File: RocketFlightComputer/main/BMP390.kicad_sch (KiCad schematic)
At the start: 5 parts

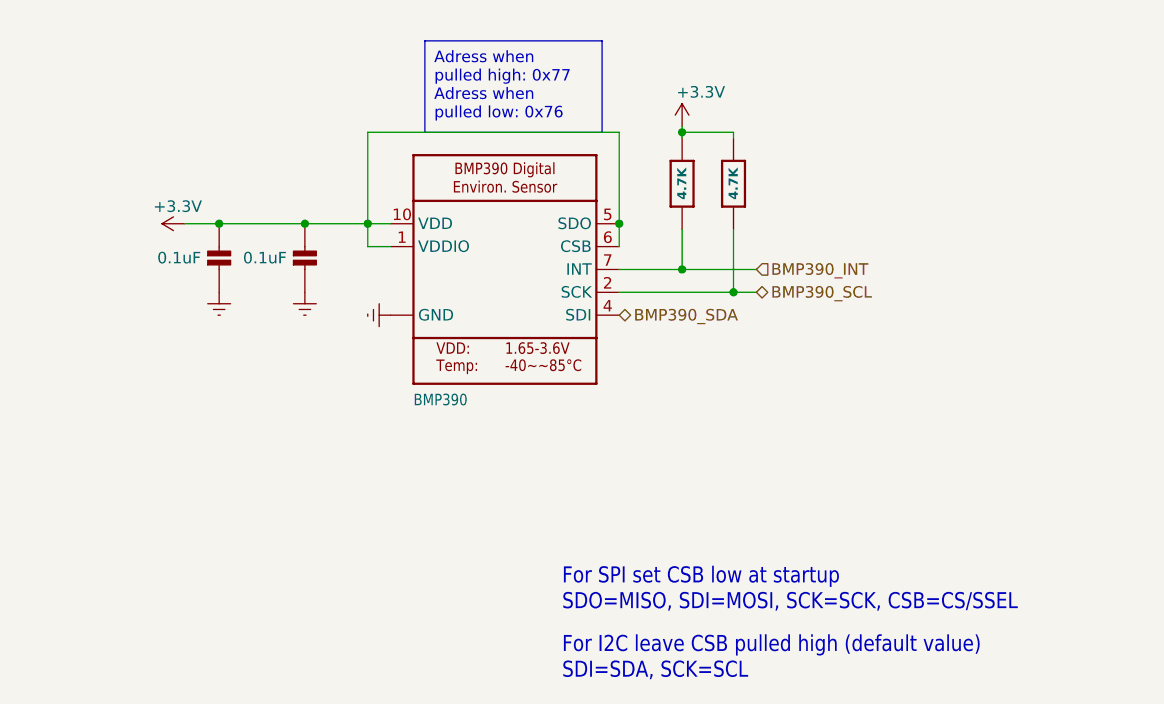
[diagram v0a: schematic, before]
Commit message: Added a few sensors schematics like multiplex for i2c comms, current/voltage sensor, micro sd slot, more to go!
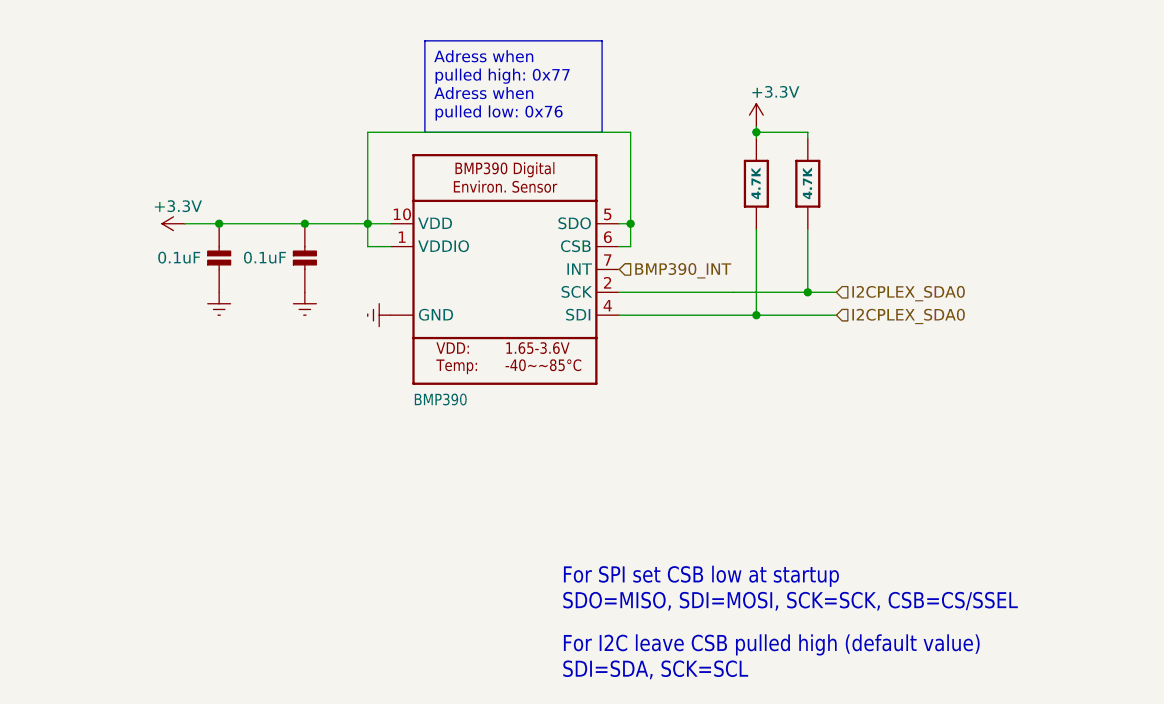
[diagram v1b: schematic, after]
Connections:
- net BMP390_SDA is gone; now on net I2CPLEX_SDA0: IC?.4 (SDI)
- net BMP390_INT: no longer R?.4 (1)
- net BMP390_SCL renamed I2CPLEX_SDA0
- net I2CPLEX_SDA0: now also R?.4 (1)
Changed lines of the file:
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@@
   (junction (at 42.545 53.34) (diameter 0) (color 0 0 0 0)
   )
-  (junction (at 86.995 53.34) (diameter 0) (color 0 0 0 0)
-  )
-  (junction (at 93.98 58.42) (diameter 0) (color 0 0 0 0)
+  (junction (at 107.95 60.96) (diameter 0) (color 0 0 0 0)
   )
   (junction (at 52.07 53.34) (diameter 0) (color 0 0 0 0)
   )
-  (junction (at 99.695 60.96) (diameter 0) (color 0 0 0 0)
-  )
   (junction (at 59.055 53.34) (diameter 0) (color 0 0 0 0)
   )
-  (junction (at 93.98 43.18) (diameter 0) (color 0 0 0 0)
+  (junction (at 88.265 53.34) (diameter 0) (color 0 0 0 0)
+  )
+  (junction (at 102.235 63.5) (diameter 0) (color 0 0 0 0)
+  )
+  (junction (at 102.235 43.18) (diameter 0) (color 0 0 0 0)
   )
   (wire (pts (xy 86.995 60.96) (xy 99.695 60.96))
     (stroke (width 0.1524) (type solid))
   )
-  (wire (pts (xy 93.98 53.975) (xy 93.98 58.42))
-    (stroke (width 0) (type default))
-  )
-  (wire (pts (xy 99.695 53.975) (xy 99.695 60.96))
-    (stroke (width 0) (type default))
-  )
-  (wire (pts (xy 93.98 58.42) (xy 102.235 58.42))
-    (stroke (width 0.1524) (type solid))
+  (wire (pts (xy 88.265 53.34) (xy 86.995 53.34))
+    (stroke (width 0) (type default))
+  )
+  (wire (pts (xy 102.235 63.5) (xy 111.125 63.5))
+    (stroke (width 0) (type default))
+  )
+  (wire (pts (xy 107.95 53.975) (xy 107.95 60.96))
+    (stroke (width 0) (type default))
   )
   (wire (pts (xy 59.055 55.88) (xy 61.595 55.88))
     (stroke (width 0.1524) (type solid))
   )
+  (wire (pts (xy 107.95 60.96) (xy 111.125 60.96))
+    (stroke (width 0) (type default))
+  )
   (wire (pts (xy 38.735 53.34) (xy 42.545 53.34))
     (stroke (width 0.1524) (type solid))
   )
-  (wire (pts (xy 86.995 43.18) (xy 59.055 43.18))
-    (stroke (width 0) (type default))
-  )
-  (wire (pts (xy 86.995 53.34) (xy 86.995 55.88))
-    (stroke (width 0) (type default))
-  )
-  (wire (pts (xy 86.995 58.42) (xy 93.98 58.42))
-    (stroke (width 0.1524) (type solid))
-  )
-  (wire (pts (xy 86.995 43.18) (xy 86.995 53.34))
-    (stroke (width 0) (type default))
-  )
-  (wire (pts (xy 93.98 43.18) (xy 93.98 43.815))
-    (stroke (width 0) (type default))
-  )
-  (wire (pts (xy 99.695 60.96) (xy 102.235 60.96))
+  (wire (pts (xy 88.265 43.18) (xy 59.055 43.18))
+    (stroke (width 0) (type default))
+  )
+  (wire (pts (xy 88.265 53.34) (xy 88.265 55.88))
+    (stroke (width 0) (type default))
+  )
+  (wire (pts (xy 88.265 43.18) (xy 88.265 53.34))
+    (stroke (width 0) (type default))
+  )
+  (wire (pts (xy 102.235 43.18) (xy 102.235 43.815))
     (stroke (width 0) (type default))
   )
@@
     (stroke (width 0.1524) (type solid))
   )
-  (wire (pts (xy 93.98 42.545) (xy 93.98 43.18))
-    (stroke (width 0) (type default))
-  )
-  (wire (pts (xy 99.695 43.18) (xy 93.98 43.18))
+  (wire (pts (xy 102.235 42.545) (xy 102.235 43.18))
+    (stroke (width 0) (type default))
+  )
+  (wire (pts (xy 107.95 43.18) (xy 102.235 43.18))
+    (stroke (width 0) (type default))
+  )
+  (wire (pts (xy 88.265 55.88) (xy 86.995 55.88))
+    (stroke (width 0) (type default))
+  )
+  (wire (pts (xy 102.235 53.975) (xy 102.235 63.5))
     (stroke (width 0) (type default))
   )
@@
     (stroke (width 0.1524) (type solid))
   )
+  (wire (pts (xy 86.995 63.5) (xy 102.235 63.5))
+    (stroke (width 0) (type default))
+  )
   (wire (pts (xy 59.055 43.18) (xy 59.055 53.34))
     (stroke (width 0) (type default))
   )
+  (wire (pts (xy 107.95 60.96) (xy 99.695 60.96))
+    (stroke (width 0) (type default))
+  )
   (wire (pts (xy 61.595 53.34) (xy 59.055 53.34))
     (stroke (width 0.1524) (type solid))
@@
     (stroke (width 0.1524) (type solid))
   )
-  (wire (pts (xy 99.695 43.815) (xy 99.695 43.18))
+  (wire (pts (xy 107.95 43.815) (xy 107.95 43.18))
     (stroke (width 0) (type default))
   )
@@
     (effects (font (size 1.778 1.5113)) (justify left bottom))
   )
-  (hierarchical_label "BMP390_INT" (shape input) (at 102.235 58.42 0) (fields_autoplaced)
+  (hierarchical_label "I2CPLEX_SDA0" (shape input) (at 111.125 60.96 0) (fields_autoplaced)
     (effects (font (size 1.27 1.27)) (justify left))
   )
-  (hierarchical_label "BMP390_SCL" (shape bidirectional) (at 102.235 60.96 0) (fields_autoplaced)
+  (hierarchical_label "BMP390_INT" (shape input) (at 86.995 58.42 0) (fields_autoplaced)
     (effects (font (size 1.27 1.27)) (justify left))
   )
-  (hierarchical_label "BMP390_SDA" (shape bidirectional) (at 86.995 63.5 0) (fields_autoplaced)
+  (hierarchical_label "I2CPLEX_SDA0" (shape input) (at 111.125 63.5 0) (fields_autoplaced)
     (effects (font (size 1.27 1.27)) (justify left))
   )
@@
     )
   )
-  (symbol (lib_id "power:+3.3V") (at 93.98 42.545 0) (unit 1)
-    (in_bom yes) (on_board yes) (dnp no)
-    (property "Reference" "#PWR063" (at 93.98 46.355 0)
-      (effects (font (size 1.27 1.27)) hide)
-    )
-    (property "Value" "+3.3V" (at 93.345 38.735 0)
+  (symbol (lib_id "power:+3.3V") (at 102.235 42.545 0) (unit 1)
+    (in_bom yes) (on_board yes) (dnp no)
+    (property "Reference" "#PWR063" (at 102.235 46.355 0)
+      (effects (font (size 1.27 1.27)) hide)
+    )
+    (property "Value" "+3.3V" (at 101.6 38.735 0)
       (effects (font (size 1.27 1.27)) (justify left))
     )
-    (property "Footprint" "" (at 93.98 42.545 0)
-      (effects (font (size 1.27 1.27)) hide)
-    )
-    (property "Datasheet" "" (at 93.98 42.545 0)
+    (property "Footprint" "" (at 102.235 42.545 0)
+      (effects (font (size 1.27 1.27)) hide)
+    )
+    (property "Datasheet" "" (at 102.235 42.545 0)
       (effects (font (size 1.27 1.27)) hide)
     )
@@
     )
   )
-  (symbol (lib_id "Adafruit_BNO08x-eagle-import:RESISTOR_4PACK") (at 93.98 48.895 90) (unit 4)
-    (in_bom yes) (on_board yes) (dnp no)
-    (property "Reference" "R?" (at 90.17 48.895 90)
-      (effects (font (size 1.27 1.27)) hide)
-    )
-    (property "Value" "4.7K" (at 93.98 48.895 0)
+  (symbol (lib_id "Adafruit_BNO08x-eagle-import:RESISTOR_4PACK") (at 102.235 48.895 90) (unit 4)
+    (in_bom yes) (on_board yes) (dnp no)
+    (property "Reference" "R?" (at 98.425 48.895 90)
+      (effects (font (size 1.27 1.27)) hide)
+    )
+    (property "Value" "4.7K" (at 102.235 48.895 0)
       (effects (font (size 1.016 1.016) bold))
     )
-    (property "Footprint" "Resistor_SMD:R_0603_1608Metric_Pad0.98x0.95mm_HandSolder" (at 93.98 48.895 0)
-      (effects (font (size 1.27 1.27)) hide)
-    )
-    (property "Datasheet" "" (at 93.98 48.895 0)
+    (property "Footprint" "Resistor_SMD:R_0603_1608Metric_Pad0.98x0.95mm_HandSolder" (at 102.235 48.895 0)
+      (effects (font (size 1.27 1.27)) hide)
+    )
+    (property "Datasheet" "" (at 102.235 48.895 0)
       (effects (font (size 1.27 1.27)) hide)
     )
@@
     )
   )
-  (symbol (lib_id "Adafruit_BNO08x-eagle-import:RESISTOR_4PACK") (at 99.695 48.895 270) (unit 3)
-    (in_bom yes) (on_board yes) (dnp no)
-    (property "Reference" "R?" (at 103.505 48.895 90)
-      (effects (font (size 1.27 1.27)) hide)
-    )
-    (property "Value" "4.7K" (at 99.695 48.895 0)
+  (symbol (lib_id "Adafruit_BNO08x-eagle-import:RESISTOR_4PACK") (at 107.95 48.895 270) (unit 3)
+    (in_bom yes) (on_board yes) (dnp no)
+    (property "Reference" "R?" (at 111.76 48.895 90)
+      (effects (font (size 1.27 1.27)) hide)
+    )
+    (property "Value" "4.7K" (at 107.95 48.895 0)
       (effects (font (size 1.016 1.016) bold))
     )
-    (property "Footprint" "Resistor_SMD:R_0603_1608Metric_Pad0.98x0.95mm_HandSolder" (at 99.695 48.895 0)
-      (effects (font (size 1.27 1.27)) hide)
-    )
-    (property "Datasheet" "" (at 99.695 48.895 0)
-      (effects (font (size 1.27 1.27)) hide)
-    )
+    (property "Footprint" "Resistor_SMD:R_0603_1608Metric_Pad0.98x0.95mm_HandSolder" (at 107.95 48.895 0)
+      (effects (font (size 1.27 1.27)) hide)
+    )
+    (property "Datasheet" "" (at 107.95 48.895 0)
+      (effects (font (size 1.27 1.27)) hide)
+    )

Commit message: Well I added a bunch of sensors, some connectors for battery, pyro channels mosfets, etc
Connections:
- net I2CPLEX_SDA0 renamed BMP390_SCL1
- net BMP390_SCL1: no longer IC?.4 (SDI), R?.4 (1)
- new net BMP390_SDA1: IC?.4 (SDI), R?.4 (1)
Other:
- note added: "Max current: 730 uA"
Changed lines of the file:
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@@
+    (effects (font (size 1.778 1.5113)) (justify left bottom))
+  )
+  (text "Max current: 730 uA\n" (at 80.645 88.9 0)
     (effects (font (size 1.778 1.5113)) (justify left bottom))
   )
@@
     (effects (font (size 1.778 1.5113)) (justify left bottom))
   )
-  (hierarchical_label "I2CPLEX_SDA0" (shape input) (at 111.125 60.96 0) (fields_autoplaced)
+  (hierarchical_label "BMP390_SCL1" (shape input) (at 111.125 60.96 0) (fields_autoplaced)
     (effects (font (size 1.27 1.27)) (justify left))
   )
@@
     (effects (font (size 1.27 1.27)) (justify left))
   )
-  (hierarchical_label "I2CPLEX_SDA0" (shape input) (at 111.125 63.5 0) (fields_autoplaced)
+  (hierarchical_label "BMP390_SDA1" (shape input) (at 111.125 63.5 0) (fields_autoplaced)
     (effects (font (size 1.27 1.27)) (justify left))
   )

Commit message: Addition of telemetry is pcb schematic
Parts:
- gave numbers to parts that had none: 4
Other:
- note added: "Max current: 0.73mA"
- note removed: "Max current: 730 uA"

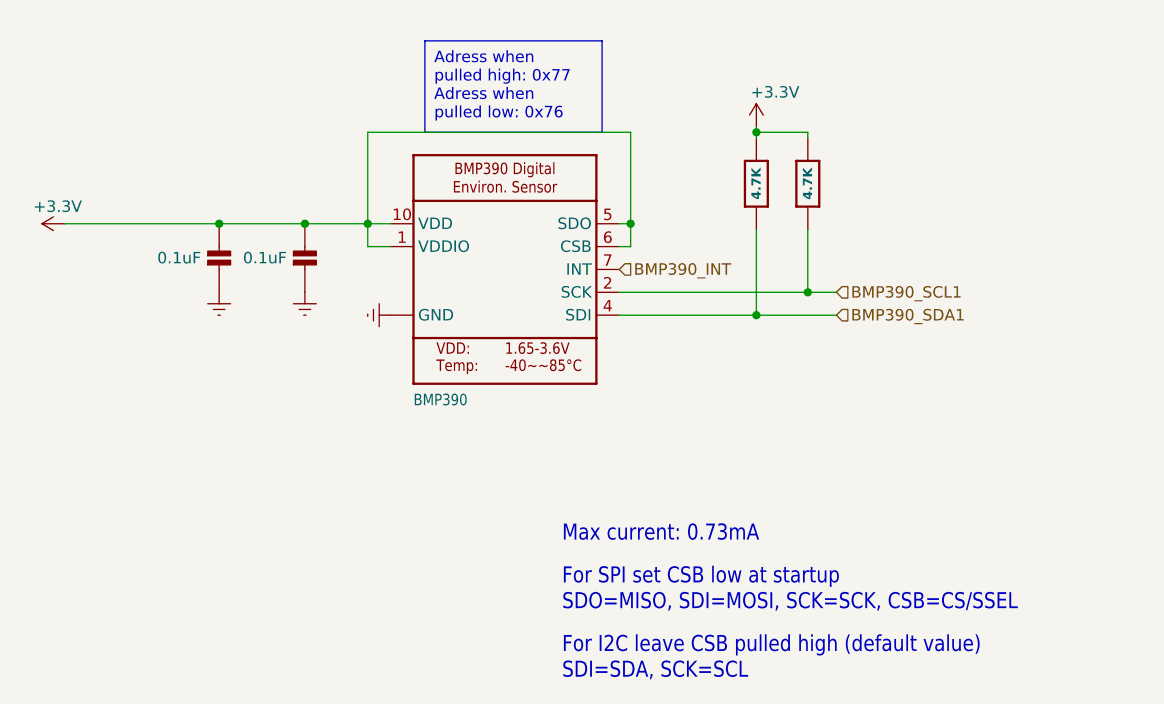
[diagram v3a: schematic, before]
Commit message: The design is getting more mature, still did not choose if doing 4 layers or 2 layers pcb, will try to add 5v for a on board camera and trace routes for reserved pins in case of usage on another vehicle
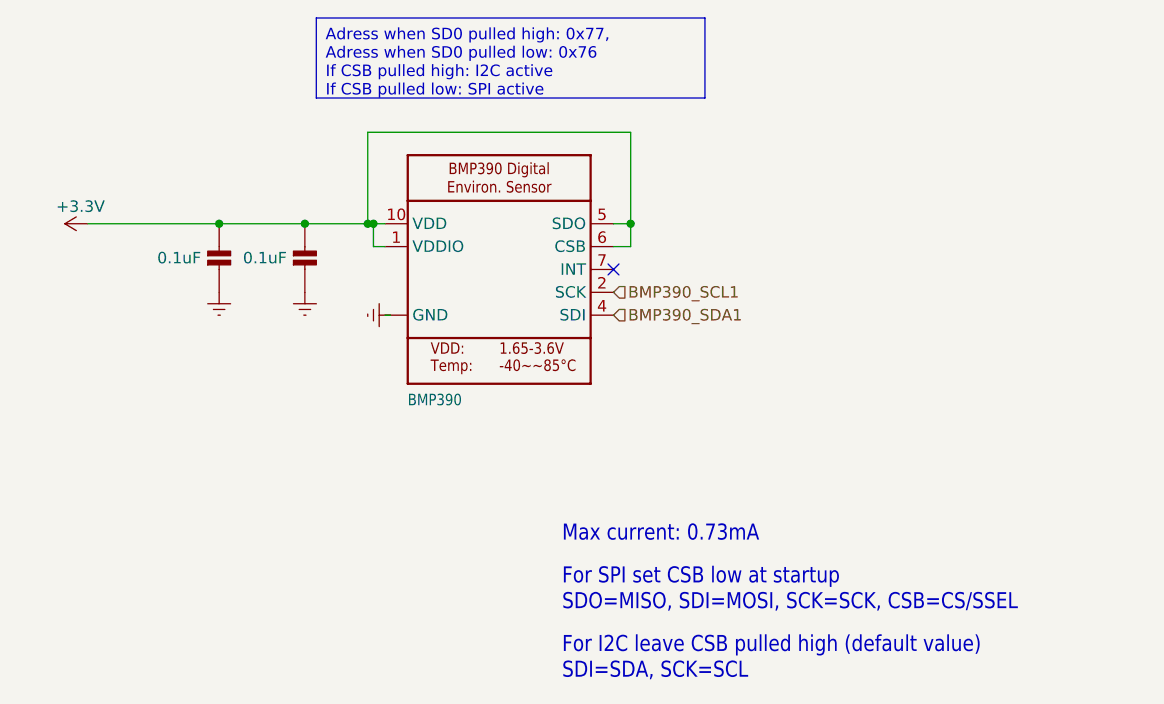
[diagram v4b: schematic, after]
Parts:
- removed R12: 4.7K, Resistor_SMD:R_0603_1608Metric_Pad0.98x0.95mm_HandSolder, symbol Adafruit_BNO08x-eagle-import:RESISTOR_4PACK
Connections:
- net BMP390_INT: no longer names the net of IC1.7 (INT)
- no-connect marks 0 -> 1

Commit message: Layout of PCB mostly done
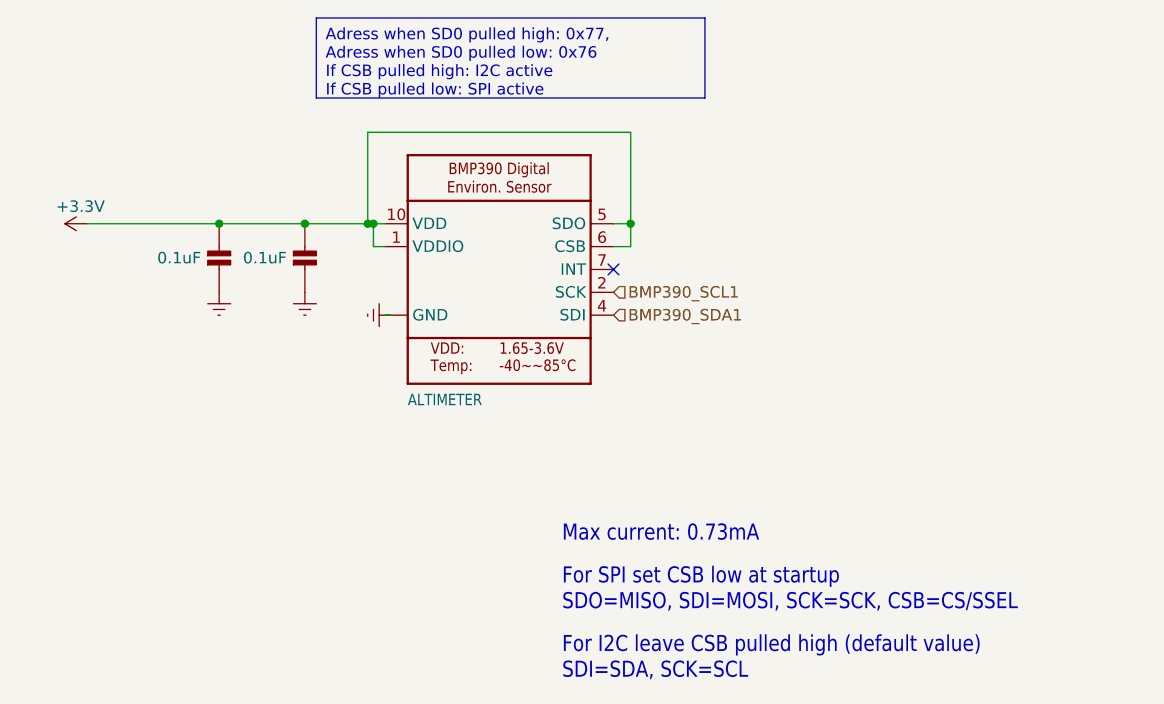
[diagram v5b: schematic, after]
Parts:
- BMP390: renamed from IC1; value BMP390 -> ALTIMETER
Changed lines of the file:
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@@
 		(on_board yes)
 		(dnp no)
-		(property "Reference" "IC1"
+		(property "Reference" "BMP390"
 			(at 63.5 44.45 0)
 			(effects
@@
 			)
 		)
-		(property "Value" "BMP390"
+		(property "Value" "ALTIMETER"
 			(at 63.5 73.66 0)
 			(effects
@@
 			(project "main"
 				(path "/27195d1d-92b2-40df-ada5-3b20841577e7/cea4c1d7-5261-445d-b36e-014b1552505a"
-					(reference "IC1")
+					(reference "BMP390")
 					(unit 1)
 				)

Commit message: Addition of all components in BOM, metal mounting plates, need to check psram if its ok for signals to pass under, all components need a double check
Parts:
- BMP1: renamed from BMP390; LCSC (none) -> C2684802; Mouser Part Number (none) -> 262-BMP390
- C34: renamed from C33; LCSC (none) -> C48579250
- C35: renamed from C34; LCSC (none) -> C48579250
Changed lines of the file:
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@@
 		(on_board yes)
 		(dnp no)
-		(property "Reference" "BMP390"
+		(property "Reference" "BMP1"
 			(at 63.5 44.45 0)
 			(effects
@@
 			)
 		)
+		(property "LCSC" "C2684802 "
+			(at 73.66 58.42 0)
+			(effects
+				(font
+					(size 1.27 1.27)
+				)
+				(hide yes)
+			)
+		)
+		(property "Mouser Part Number" "262-BMP390"
+			(at 73.66 58.42 0)
+			(effects
+				(font
+					(size 1.27 1.27)
+				)
+				(hide yes)
+			)
+		)
 		(pin "1"
 		)
@@
 			(project "main"
 				(path "/27195d1d-92b2-40df-ada5-3b20841577e7/cea4c1d7-5261-445d-b36e-014b1552505a"
-					(reference "BMP390")
+					(reference "BMP1")
 					(unit 1)
 				)
@@
 		(on_board yes)
 		(dnp no)
-		(property "Reference" "C34"
+		(property "Reference" "C35"
 			(at 49.78 57.17 0)
 			(effects
@@
 			)
 		)
+		(property "LCSC" "C48579250"
+			(at 52.07 58.42 0)
+			(effects
+				(font
+					(size 1.27 1.27)
+				)
+				(hide yes)
+			)
+		)
 		(pin "1"
 		)
@@
 			(project "main"
 				(path "/27195d1d-92b2-40df-ada5-3b20841577e7/cea4c1d7-5261-445d-b36e-014b1552505a"
-					(reference "C34")
+					(reference "C35")
 					(unit 1)
 				)
@@
 		(on_board yes)
 		(dnp no)
-		(property "Reference" "#PWR0148"
+		(property "Reference" "#PWR092"
 			(at 31.75 53.34 0)
 			(effects
@@
 			(project "main"
 				(path "/27195d1d-92b2-40df-ada5-3b20841577e7/cea4c1d7-5261-445d-b36e-014b1552505a"
-					(reference "#PWR0148")
+					(reference "#PWR092")
 					(unit 1)
 				)
@@
 		(dnp no)
 		(fields_autoplaced yes)
-		(property "Reference" "#PWR085"
+		(property "Reference" "#PWR093"
 			(at 42.545 67.31 0)
 			(effects
@@
 			(project "main"
 				(path "/27195d1d-92b2-40df-ada5-3b20841577e7/cea4c1d7-5261-445d-b36e-014b1552505a"
-					(reference "#PWR085")
+					(reference "#PWR093")
 					(unit 1)
 				)
@@
 		(dnp no)
 		(fields_autoplaced yes)
-		(property "Reference" "#PWR087"
+		(property "Reference" "#PWR095"
 			(at 55.245 63.5 0)
 			(effects
@@
 			(project "main"
 				(path "/27195d1d-92b2-40df-ada5-3b20841577e7/cea4c1d7-5261-445d-b36e-014b1552505a"
-					(reference "#PWR087")
+					(reference "#PWR095")
 					(unit 1)
 				)
@@
 		(dnp no)
 		(fields_autoplaced yes)
-		(property "Reference" "#PWR086"
+		(property "Reference" "#PWR094"
 			(at 52.07 67.31 0)
 			(effects
@@
 			(project "main"
 				(path "/27195d1d-92b2-40df-ada5-3b20841577e7/cea4c1d7-5261-445d-b36e-014b1552505a"
-					(reference "#PWR086")
+					(reference "#PWR094")
 					(unit 1)
 				)
@@
 		(on_board yes)
 		(dnp no)
-		(property "Reference" "C33"
+		(property "Reference" "C34"
 			(at 40.255 57.17 0)
 			(effects
@@
 			)
 		)
+		(property "LCSC" "C48579250"
+			(at 42.545 58.42 0)
+			(effects
+				(font
+					(size 1.27 1.27)
+				)
+				(hide yes)
+			)
+		)
 		(pin "1"
 		)
@@
 			(project "main"
 				(path "/27195d1d-92b2-40df-ada5-3b20841577e7/cea4c1d7-5261-445d-b36e-014b1552505a"
-					(reference "C33")
-					(unit 1)
-				)
+					(reference "C34")
+					(unit 1)
+				)
